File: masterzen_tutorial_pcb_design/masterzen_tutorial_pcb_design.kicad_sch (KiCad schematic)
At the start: 12 parts, among them J1 AVR-ISP-6, U1 ATmega32U4-A, Y1 Crystal_GND24_Small

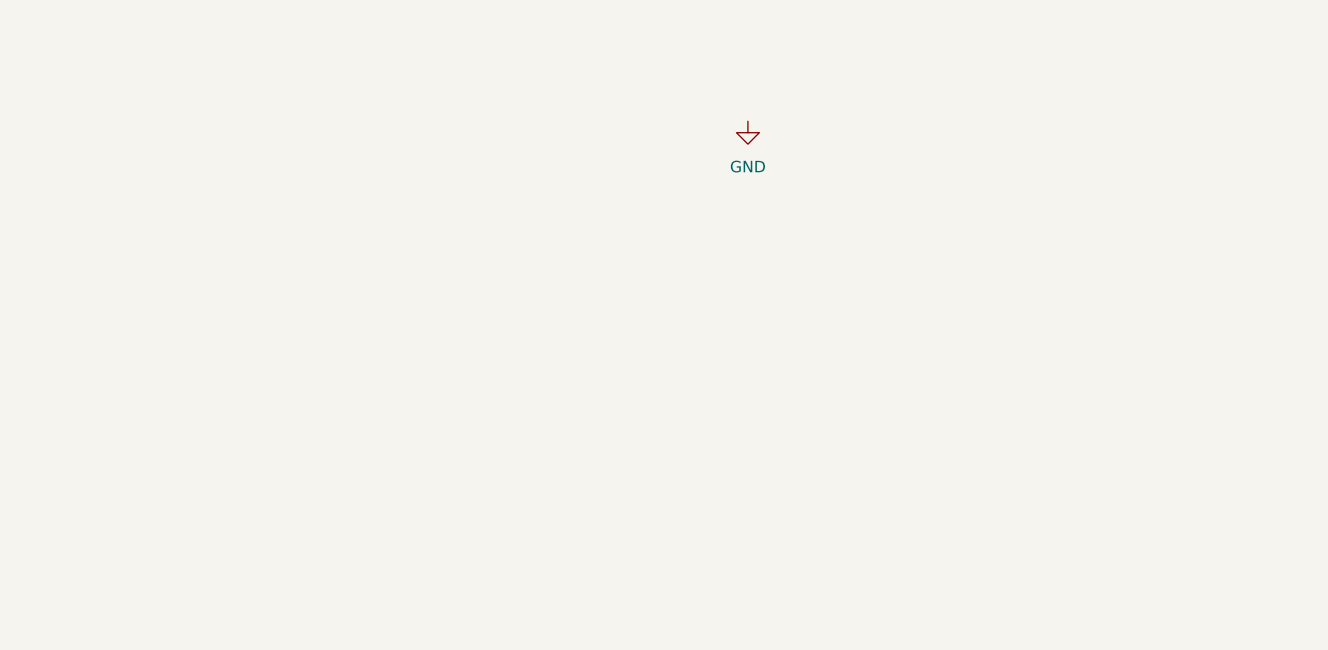
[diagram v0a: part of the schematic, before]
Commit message: moved submodules and added reeset button
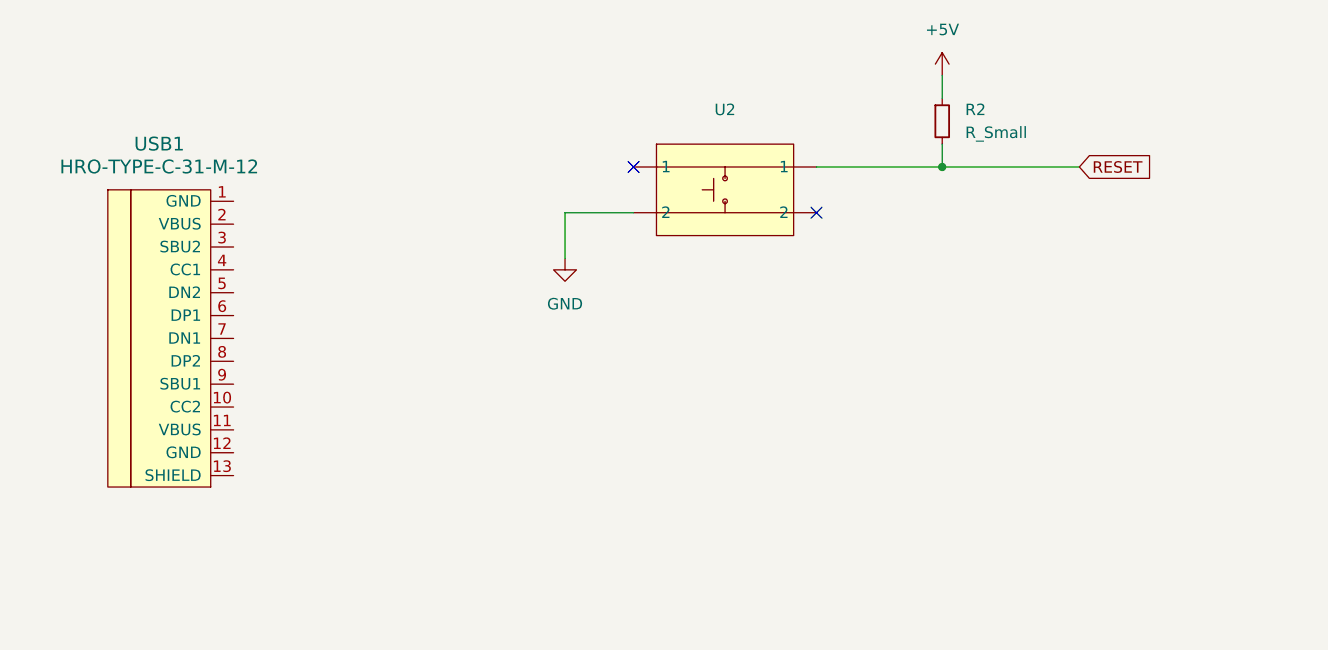
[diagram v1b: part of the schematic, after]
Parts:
- added R2: R_Small, symbol Device:R_Small
- added U2: ~, symbol SW_PUSH:SW_SKQG
- added USB1: HRO-TYPE-C-31-M-12, symbol Type-C:HRO-TYPE-C-31-M-12
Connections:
- net +5V: now also R2.1
- net GND: now also U2. (2)
- net RESET: now also R2.2, U2. (2)
- no-connect marks 1 -> 3
